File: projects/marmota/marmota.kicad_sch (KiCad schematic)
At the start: 23 parts, among them J1 USB_C, J2 Conn_01x20_Pin, J3 Conn_01x20_Pin, J4 TC2030-NL, J5 Conn_01x04_MountingPin, J6 Conn_01x04_MountingPin, SW1 Button top, SW2 Button side, U6 nRF52840_E73-2G4M08S1C, U7 nPM1300-QEXX, Y1 32.768KHz

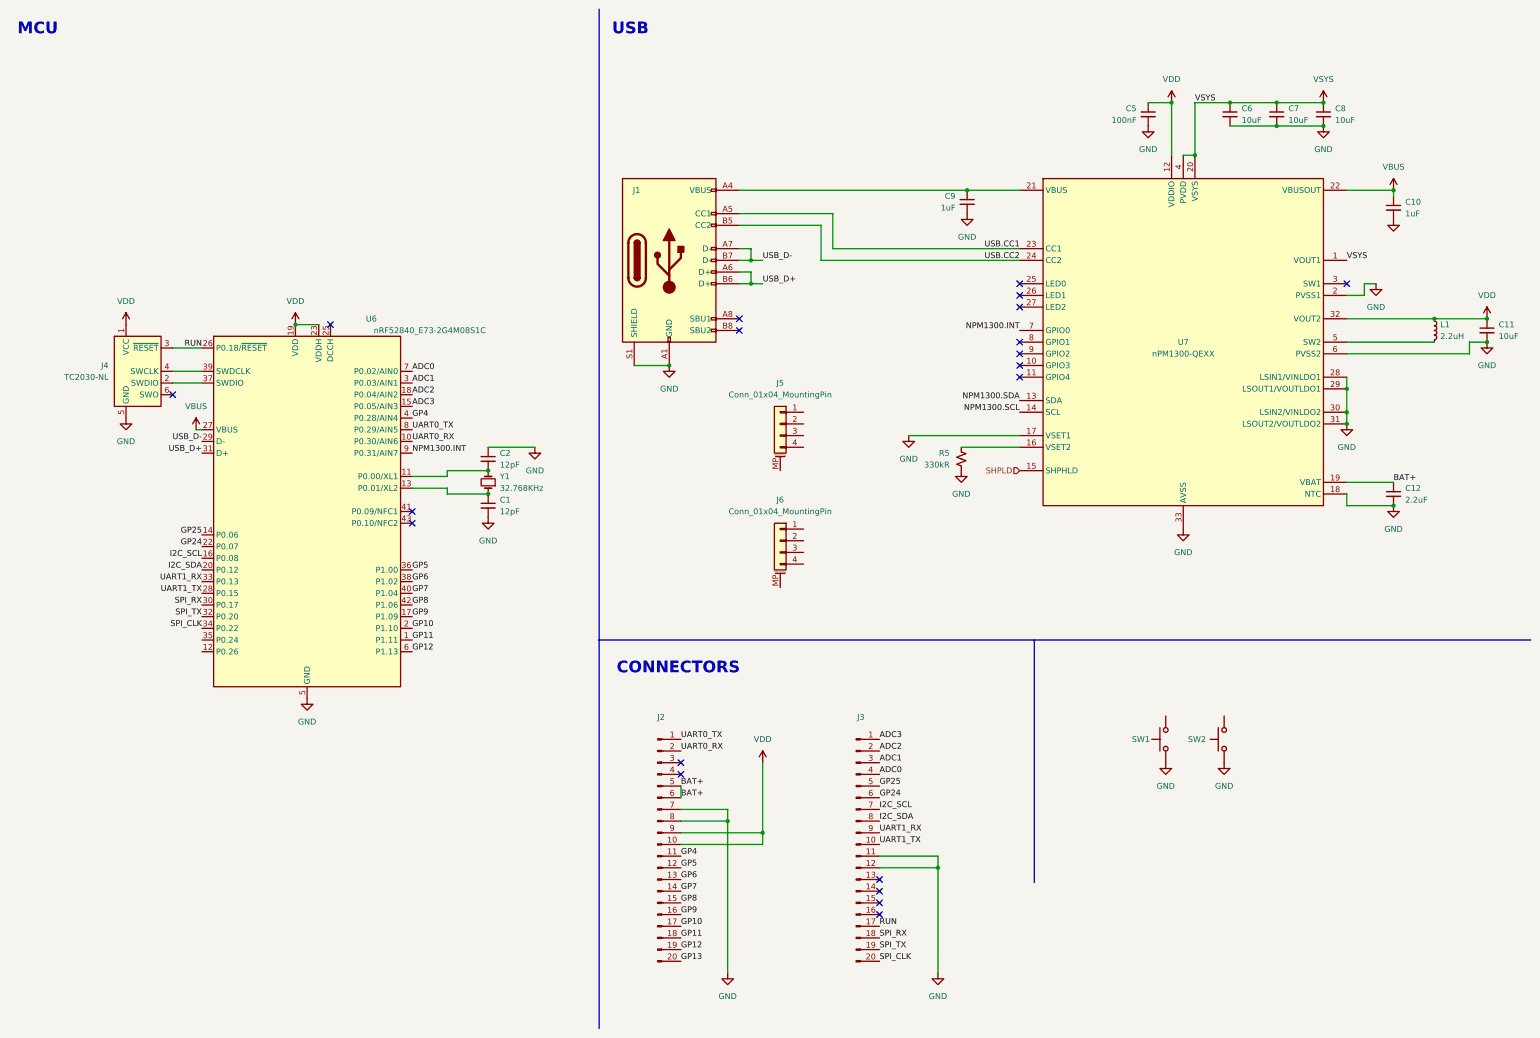
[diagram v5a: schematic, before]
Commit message: Updated for nRF52840
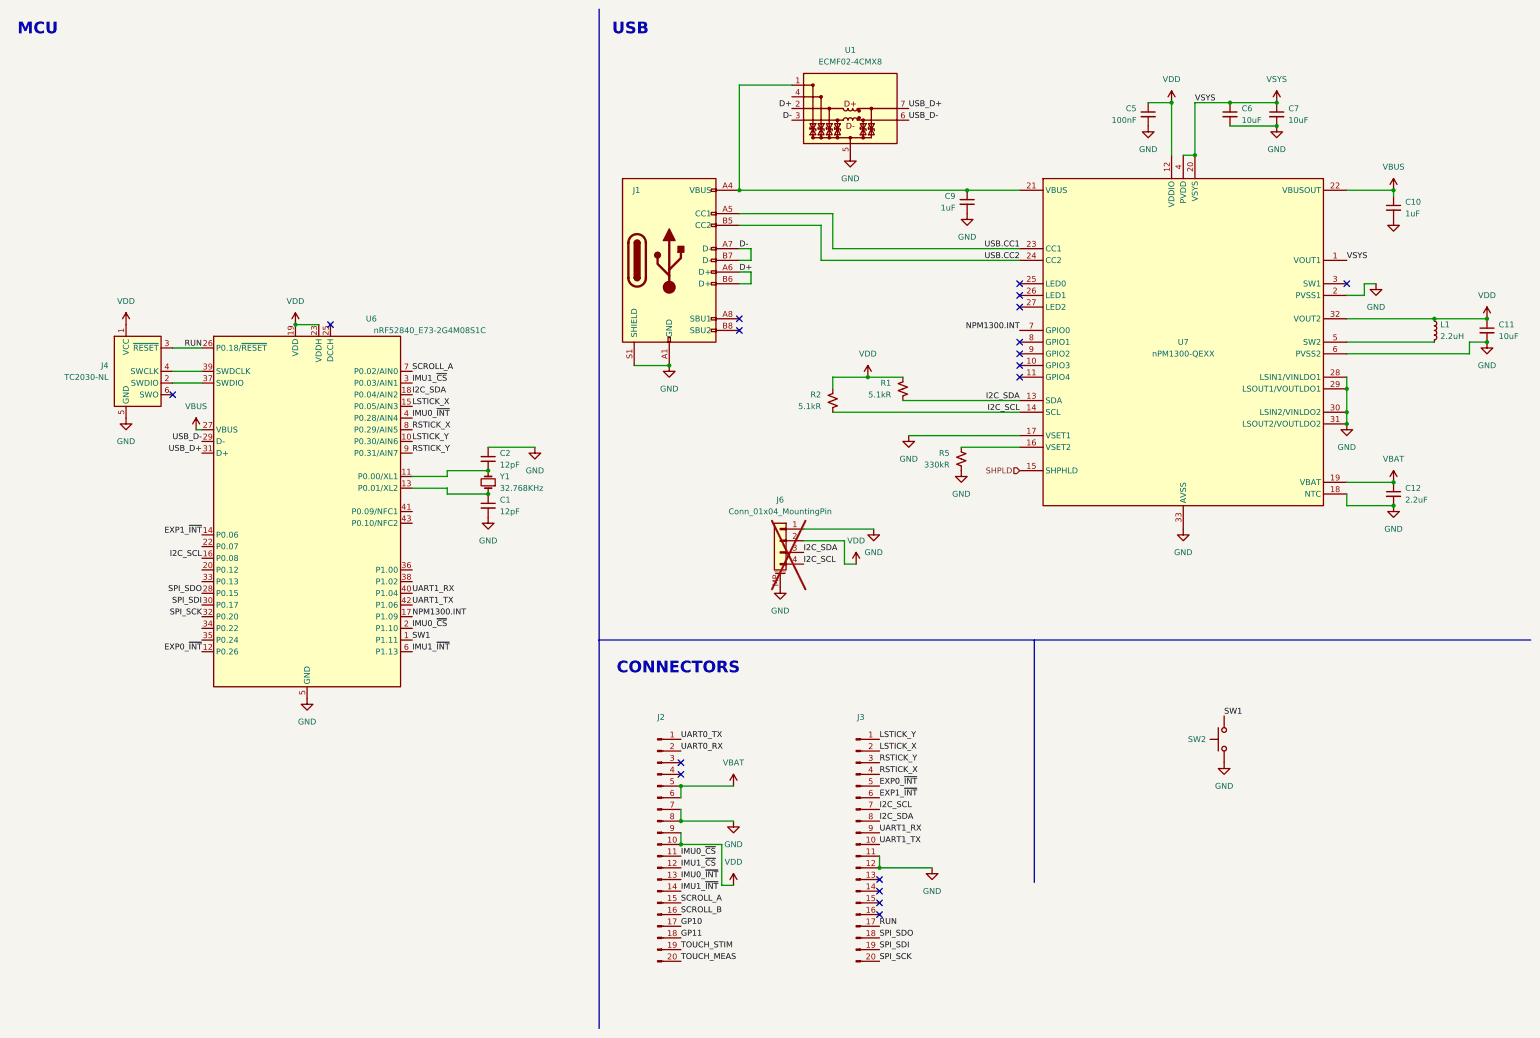
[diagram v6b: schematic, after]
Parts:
- removed C8: 10uF, Capacitor_SMD:C_0603_1608Metric, symbol Device:C_Small
- removed J5: Conn_01x04_MountingPin, Connector_JST:JST_SH_SM04B-SRSS-TB_1x04-1MP_P1.00mm_Horizontal, symbol Connector_Generic_MountingPin:Conn_01x04_MountingPin
- removed SW1: Button top, ILO_fp:Alpsalpine_SKRP_compact, symbol Switch:SW_Push
- added R1, R2: 5.1kR, Resistor_SMD:R_0402_1005Metric, symbol Device:R_Small_US
- added U1: ECMF02-4CMX8, hlord2000-Package_DFN_QFN:ST_UQFN-8L_1.2x2.5mm_P0.5mm, symbol hlord2000-Power_Protection:ECMF02-4CMX8
- C1, C2: footprint (none) -> Capacitor_SMD:C_0402_1005Metric
- J6: now not fitted; now left out of the parts list
- Y1: footprint (none) -> Crystal:Crystal_SMD_2012-2Pin_2.0x1.2mm
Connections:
- net NPM1300.SCL is gone; now on net I2C_SCL: U7.14 (SCL)
- net NPM1300.SDA is gone; now on net I2C_SDA: U7.13 (SDA)
- net GND: now also J6.1 (Pin_1), J6.MP (MountPin), U1.5 (GND), U1.8 (GND)
- net GP10: no longer U6.2 (P1.10)
- net GP11: no longer U6.1 (P1.11)
- net I2C_SCL: now also J6.4 (Pin_4), R2.2
- net I2C_SDA: now also J6.3 (Pin_3), U6.18 (P0.04/AIN2), R1.2; no longer U6.20 (P0.12)
- net NPM1300.INT: now also U6.17 (P1.09); no longer U6.9 (P0.31/AIN7)
- net UART0_RX: no longer U6.10 (P0.30/AIN6)
- net UART0_TX: no longer U6.8 (P0.29/AIN5)
- net UART1_RX: now also U6.40 (P1.04); no longer U6.33 (P0.13)
- net UART1_TX: now also U6.42 (P1.06); no longer U6.28 (P0.15)
- net USB_D+: now also U1.7 (D-_out); no longer J1.A6 (D+), J1.B6 (D+)
- net USB_D-: now also U1.6 (D+_out); no longer J1.A7 (D-), J1.B7 (D-)
- net VDD: now also J6.2 (Pin_2), R1.1, R2.1
- net SW1: now reaches SW2.2
- net SW1: now also U6.1 (P1.11)
- net at C9.1, J1.A4 (VBUS), J1.A9 (VBUS)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: now also U1.1 (VBUS)
- net EXP0_~{INT}: now reaches U6.12 (P0.26)
- net EXP0_~{INT}: now also J3.5 (Pin_5)
- net ADC0 renamed RSTICK_X
- net RSTICK_X: now also U6.8 (P0.29/AIN5); no longer U6.7 (P0.02/AIN0)
- net ADC1 renamed IMU1_~{CS}
- net IMU1_~{CS}: now also J2.12 (Pin_12); no longer J3.3 (Pin_3)
- net ADC2 renamed LSTICK_X
- net LSTICK_X: now also U6.15 (P0.05/AIN3); no longer U6.18 (P0.04/AIN2)
- net ADC3 renamed LSTICK_Y
- net LSTICK_Y: now also U6.10 (P0.30/AIN6); no longer U6.15 (P0.05/AIN3)
- net BAT+ renamed VBAT
- net GP12 renamed IMU1_~{INT}
- net IMU1_~{INT}: now also J2.14 (Pin_14); no longer J2.19 (Pin_19)
- net GP13 renamed TOUCH_MEAS
- net GP24: no longer names the net of U6.22 (P0.07)
- net GP24: no longer J3.6 (Pin_6)
- net GP25 renamed EXP1_~{INT}
- net EXP1_~{INT}: now also J3.6 (Pin_6); no longer J3.5 (Pin_5)
- net GP4 renamed IMU0_~{CS}
- net IMU0_~{CS}: now also U6.2 (P1.10); no longer U6.4 (P0.28/AIN4)
- net GP5: no longer names the net of U6.36 (P1.00)
- net GP5: no longer J2.12 (Pin_12)
- net GP6: no longer names the net of U6.38 (P1.02)
- net GP6: no longer J2.13 (Pin_13)
- removed net GP7: J2.14 (Pin_14), U6.40 (P1.04)
- net GP8 renamed SCROLL_A
- net SCROLL_A: now also U6.7 (P0.02/AIN0); no longer U6.42 (P1.06)
- net GP9 renamed SCROLL_B
- net SCROLL_B: no longer U6.17 (P1.09)
- net SPI_CLK: no longer names the net of U6.34 (P0.22)
- net SPI_CLK: no longer J3.20 (Pin_20)
- net SPI_RX renamed SPI_SDI
- net SPI_SDI: now also J3.19 (Pin_19); no longer J3.18 (Pin_18)
- net SPI_TX renamed SPI_SCK
- net SPI_SCK: now also J3.20 (Pin_20); no longer J3.19 (Pin_19)
- new net D+: J1.A6 (D+), J1.B6 (D+), U1.2 (D-_in)
- new net D-: J1.A7 (D-), J1.B7 (D-), U1.3 (D+_in)
- new net IMU0_~{INT}: J2.13 (Pin_13), U6.4 (P0.28/AIN4)
- new net RSTICK_Y: J3.3 (Pin_3), U6.9 (P0.31/AIN7)
- new net SPI_SDO: J3.18 (Pin_18), U6.28 (P0.15)
- new net TOUCH_STIM: J2.19 (Pin_19)
- no-connect marks 20 -> 18
